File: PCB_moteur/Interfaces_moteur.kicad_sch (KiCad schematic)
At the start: 20 parts, among them J3 Conn_01x02, J4 SYS_SW_Conn_01x05_Header, J5 Conn_01x04_Socket, J7 Conn_02x06_Top_Bottom, U2 ISOW1044, U4 LSF0204PWR, U9 INA333xxDGK

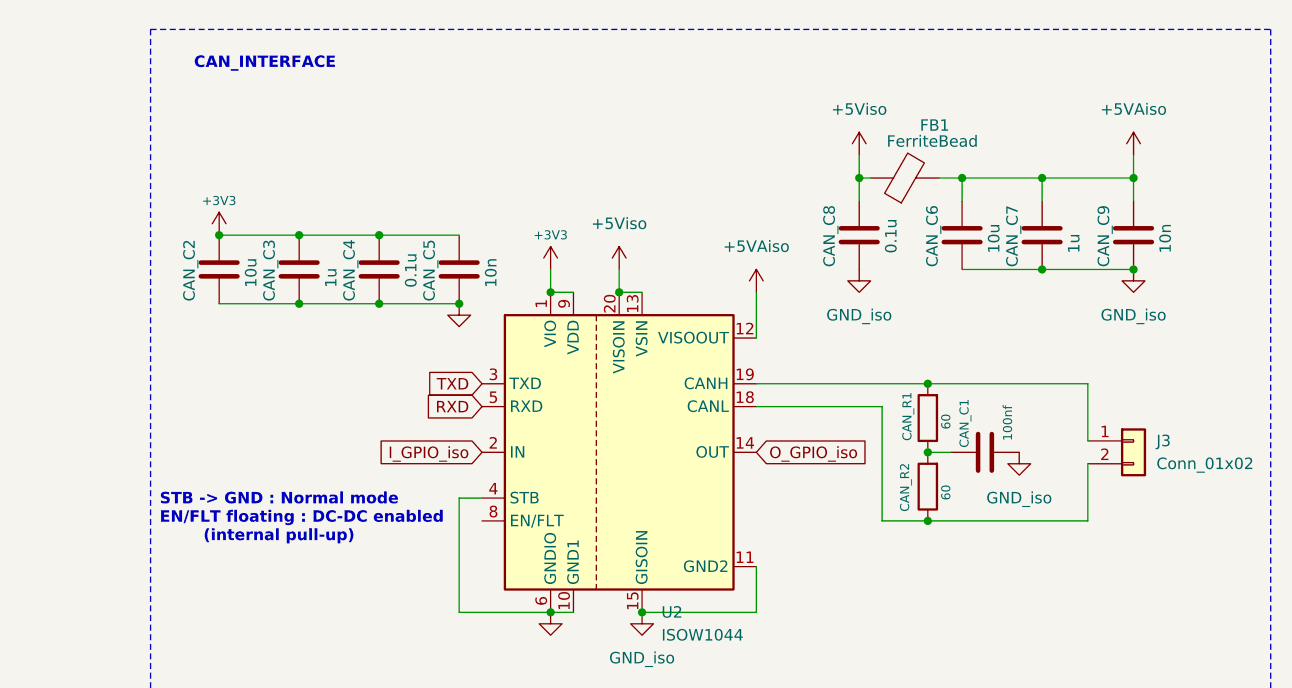
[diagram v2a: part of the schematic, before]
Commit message: wip: change 4 pyros -> 2 pyros
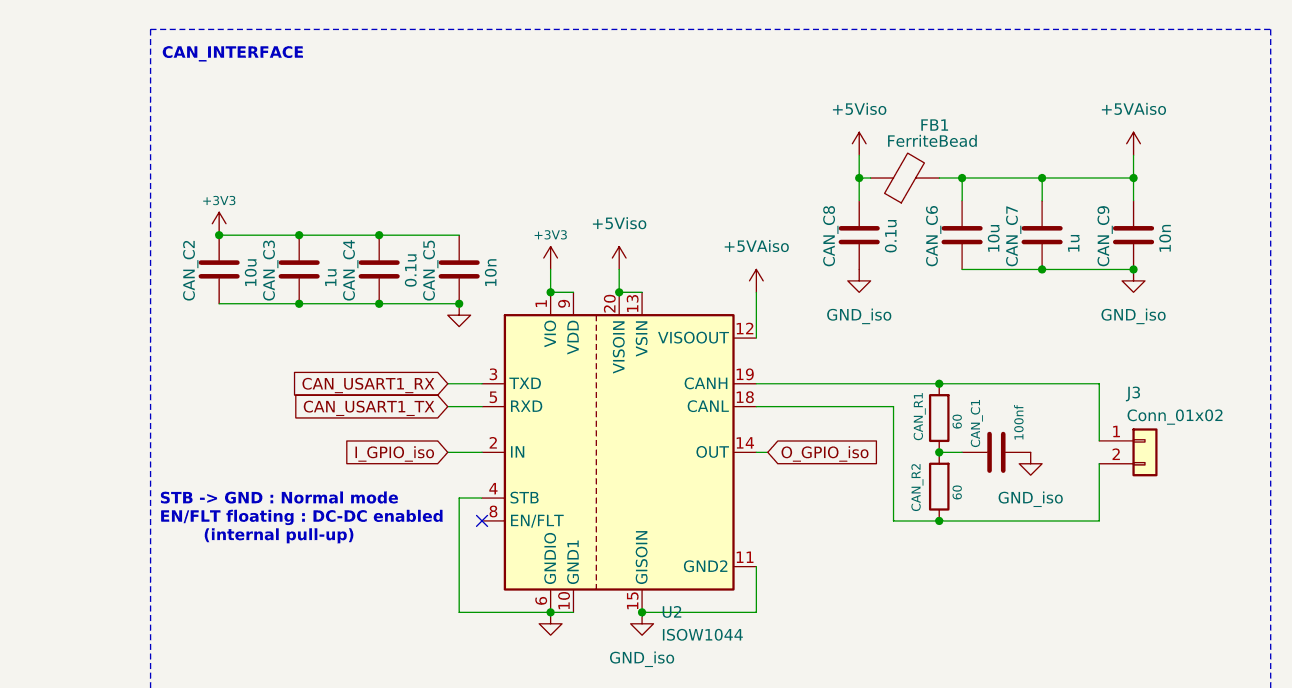
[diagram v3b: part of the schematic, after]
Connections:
- net RXD renamed CAN_USART1_TX
- net TXD renamed CAN_USART1_RX
- no-connect marks 0 -> 1
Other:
- moved on the sheet: CAN_C1, CAN_R1, CAN_R2, J3
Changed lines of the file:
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@@
 	(text "CAN_INTERFACE"
 		(exclude_from_sim no)
-		(at 162.306 40.132 0)
+		(at 158.75 39.116 0)
 		(effects
 			(font
@@
 	)
 	(junction
-		(at 243.84 82.55)
+		(at 245.11 82.55)
 		(diameter 0)
 		(color 0 0 0 0)
@@
 	)
 	(junction
-		(at 243.84 74.93)
+		(at 245.11 74.93)
 		(diameter 0)
 		(color 0 0 0 0)
@@
 	)
 	(junction
-		(at 243.84 90.17)
+		(at 245.11 90.17)
 		(diameter 0)
 		(color 0 0 0 0)
@@
 		(color 0 0 0 0)
 	)
+	(no_connect
+		(at 194.31 90.17)
+	)
 	(wire
 		(pts
@@
 	(wire
 		(pts
-			(xy 243.84 82.55) (xy 246.38 82.55)
+			(xy 245.11 82.55) (xy 247.65 82.55)
 		)
 		(stroke
@@
 	(wire
 		(pts
-			(xy 224.79 77.47) (xy 238.76 77.47)
+			(xy 224.79 77.47) (xy 240.03 77.47)
 		)
 		(stroke
@@
 	(wire
 		(pts
+			(xy 190.5 77.47) (xy 194.31 77.47)
+		)
+		(stroke
+			(width 0)
+			(type default)
+		)
+	)
+	(wire
+		(pts
 			(xy 60.96 102.87) (xy 64.77 102.87)
 		)
@@
 	(wire
 		(pts
-			(xy 238.76 77.47) (xy 238.76 90.17)
+			(xy 240.03 77.47) (xy 240.03 90.17)
 		)
 		(stroke
@@
 	(wire
 		(pts
-			(xy 243.84 74.93) (xy 261.62 74.93)
+			(xy 245.11 74.93) (xy 262.89 74.93)
 		)
 		(stroke
@@
 	(wire
 		(pts
+			(xy 226.06 82.55) (xy 224.79 82.55)
+		)
+		(stroke
+			(width 0)
+			(type default)
+		)
+	)
+	(wire
+		(pts
 			(xy 55.88 152.4) (xy 59.69 152.4)
 		)
@@
 	(wire
 		(pts
+			(xy 190.5 82.55) (xy 194.31 82.55)
+		)
+		(stroke
+			(width 0)
+			(type default)
+		)
+	)
+	(wire
+		(pts
 			(xy 81.28 102.87) (xy 77.47 102.87)
 		)
@@
 	(wire
 		(pts
-			(xy 224.79 74.93) (xy 243.84 74.93)
+			(xy 224.79 74.93) (xy 245.11 74.93)
 		)
 		(stroke
@@
 	(wire
 		(pts
-			(xy 261.62 90.17) (xy 261.62 83.82)
+			(xy 262.89 90.17) (xy 262.89 83.82)
 		)
 		(stroke
@@
 	(wire
 		(pts
+			(xy 190.5 74.93) (xy 194.31 74.93)
+		)
+		(stroke
+			(width 0)
+			(type default)
+		)
+	)
+	(wire
+		(pts
 			(xy 231.14 152.4) (xy 231.14 147.32)
 		)
@@
 	(wire
 		(pts
-			(xy 238.76 90.17) (xy 243.84 90.17)
+			(xy 240.03 90.17) (xy 245.11 90.17)
 		)
 		(stroke
@@
 	(wire
 		(pts
-			(xy 261.62 81.28) (xy 261.62 74.93)
+			(xy 262.89 81.28) (xy 262.89 74.93)
 		)
 		(stroke
@@
 	(wire
 		(pts
-			(xy 243.84 90.17) (xy 261.62 90.17)
+			(xy 245.11 90.17) (xy 262.89 90.17)
 		)
 		(stroke
@@
 		)
 	)
-	(global_label "TXD"
+	(global_label "CAN_USART1_RX"
 		(shape input)
-		(at 194.31 74.93 180)
+		(at 190.5 74.93 180)
 		(fields_autoplaced yes)
 		(effects
@@
 		)
 		(property "Intersheetrefs" "${INTERSHEET_REFS}"
-			(at 187.8777 74.93 0)
+			(at 172.3353 74.93 0)
 			(effects
 				(font
@@
 	(global_label "I_GPIO_iso"
 		(shape input)
-		(at 194.31 82.55 180)
+		(at 190.5 82.55 180)
 		(fields_autoplaced yes)
 		(effects
@@
 		)
 		(property "Intersheetrefs" "${INTERSHEET_REFS}"
-			(at 181.5276 82.55 0)
+			(at 177.7176 82.55 0)
 			(effects
 				(font
@@
 	(global_label "O_GPIO_iso"
 		(shape input)
-		(at 224.79 82.55 0)
+		(at 226.06 82.55 0)
 		(fields_autoplaced yes)
 		(effects
@@
 		)
 		(property "Intersheetrefs" "${INTERSHEET_REFS}"
-			(at 238.2981 82.55 0)
+			(at 239.5681 82.55 0)
 			(effects
 				(font
@@
 		)
 	)
-	(global_label "RXD"
+	(global_label "CAN_USART1_TX"
 		(shape input)
-		(at 194.31 77.47 180)
+		(at 190.5 77.47 180)
 		(fields_autoplaced yes)
 		(effects
@@
 		)
 		(property "Intersheetrefs" "${INTERSHEET_REFS}"
-			(at 187.5753 77.47 0)
+			(at 172.6377 77.47 0)
 			(effects
 				(font
@@
 	(symbol
 		(lib_id "Device:R")
-		(at 243.84 86.36 180)
+		(at 245.11 86.36 180)
 		(unit 1)
 		(exclude_from_sim no)
@@
 		(dnp no)
 		(property "Reference" "CAN_R2"
-			(at 241.3 89.154 90)
+			(at 242.57 89.154 90)
 			(effects
 				(font
@@
 		)
 		(property "Value" "60"
-			(at 245.872 87.884 90)
+			(at 247.142 87.884 90)
 			(effects
 				(font
@@
 		)
 		(property "Footprint" "Resistor_SMD:R_0805_2012Metric"
-			(at 245.618 86.36 90)
+			(at 246.888 86.36 90)
 			(effects
 				(font
@@
 		)
 		(property "Datasheet" "~"
-			(at 243.84 86.36 0)
+			(at 245.11 86.36 0)
 			(effects
 				(font
@@
 		)
 		(property "Description" ""
-			(at 243.84 86.36 0)
+			(at 245.11 86.36 0)
 			(effects
 				(font
@@
 	(symbol
 		(lib_id "power:GND1")
-		(at 254 82.55 0)
+		(at 255.27 82.55 0)
 		(unit 1)
 		(exclude_from_sim no)
@@
 		(fields_autoplaced yes)
 		(property "Reference" "#PWR014"
-			(at 254 88.9 0)
+			(at 255.27 88.9 0)
 			(effects
 				(font
@@
 		)
 		(property "Value" "GND_iso"
-			(at 254 87.63 0)
+			(at 255.27 87.63 0)
 			(effects
 				(font
@@
 		)
 		(property "Footprint" ""
-			(at 254 82.55 0)
+			(at 255.27 82.55 0)
 			(effects
 				(font
@@
 		)
 		(property "Datasheet" ""
-			(at 254 82.55 0)
+			(at 255.27 82.55 0)
 			(effects
 				(font
@@
 		)
 		(property "Description" "Power symbol creates a global label with name \"GND1\" , ground"
-			(at 254 82.55 0)
+			(at 255.27 82.55 0)
 			(effects
 				(font
@@
 	(symbol
 		(lib_id "Device:R")
-		(at 243.84 78.74 180)
+		(at 245.11 78.74 180)
 		(unit 1)
 		(exclude_from_sim no)
@@
 		(dnp no)
 		(property "Reference" "CAN_R1"
-			(at 241.554 81.28 90)
+			(at 242.824 81.28 90)
 			(effects
 				(font
@@
 		)
 		(property "Value" "60"
-			(at 245.872 80.01 90)
+			(at 247.142 80.01 90)
 			(effects
 				(font
@@
 		)
 		(property "Footprint" "Resistor_SMD:R_0805_2012Metric"
-			(at 245.618 78.74 90)
+			(at 246.888 78.74 90)
 			(effects
 				(font
@@
 		)
 		(property "Datasheet" "~"
-			(at 243.84 78.74 0)
+			(at 245.11 78.74 0)
 			(effects
 				(font
@@
 		)
 		(property "Description" ""
-			(at 243.84 78.74 0)
+			(at 245.11 78.74 0)
 			(effects
 				(font
@@
 	(symbol
 		(lib_id "Connector_Generic:Conn_01x02")
-		(at 266.7 81.28 0)
+		(at 267.97 81.28 0)
 		(unit 1)
 		(exclude_from_sim no)
@@
 		(on_board yes)
 		(dnp no)
-		(fields_autoplaced yes)
 		(property "Reference" "J3"
-			(at 269.24 81.2799 0)
+			(at 265.938 75.946 0)
 			(effects
 				(font
@@
 		)
 		(property "Value" "Conn_01x02"
-			(at 269.24 83.8199 0)
+			(at 265.938 78.486 0)
 			(effects
 				(font
@@
 		)
 		(property "Footprint" ""
-			(at 266.7 81.28 0)
+			(at 267.97 81.28 0)
 			(effects
 				(font
@@
 		)
 		(property "Datasheet" "~"
-			(at 266.7 81.28 0)
+			(at 267.97 81.28 0)
 			(effects
 				(font
@@
 		)
 		(property "Description" "Generic connector, single row, 01x02, script generated (kicad-library-utils/schlib/autogen/connector/)"
-			(at 266.7 81.28 0)
+			(at 267.97 81.28 0)
 			(effects
 				(font
@@
 	(symbol
 		(lib_id "Device:C")
-		(at 250.19 82.55 90)
+		(at 251.46 82.55 90)
 		(unit 1)
 		(exclude_from_sim no)
@@
 		(dnp no)
 		(property "Reference" "CAN_C1"
-			(at 247.904 82.042 0)
+			(at 249.174 82.042 0)
 			(effects
 				(font
@@
 		)
 		(property "Value" "100nf"
-			(at 252.73 81.28 0)
+			(at 254 81.28 0)
 			(effects
 				(font
@@
 		)
 		(property "Footprint" "Capacitor_SMD:C_0805_2012Metric"
-			(at 254 81.5848 0)
+			(at 255.27 81.5848 0)
 			(effects
 				(font
@@
 		)
 		(property "Datasheet" "~"
-			(at 250.19 82.55 0)
+			(at 251.46 82.55 0)
 			(effects
 				(font
@@
 		)
 		(property "Description" ""
-			(at 250.19 82.55 0)
+			(at 251.46 82.55 0)
 			(effects
 				(font

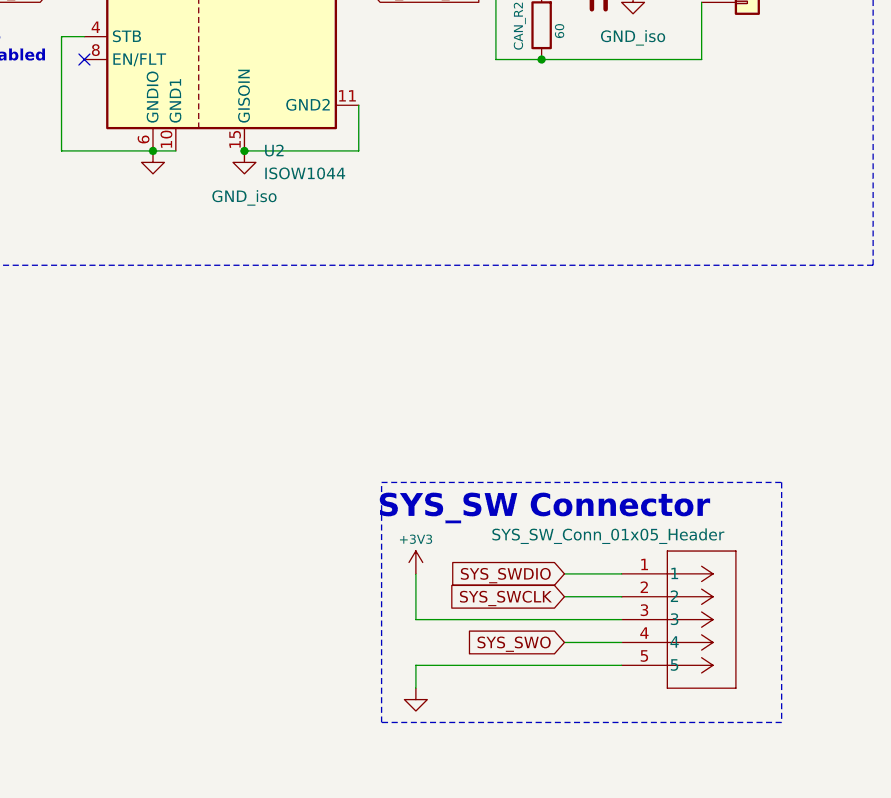
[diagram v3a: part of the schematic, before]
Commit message: fix: power supply + add LED RG + add mounting holes + change 6pins header SWD connector + pyros
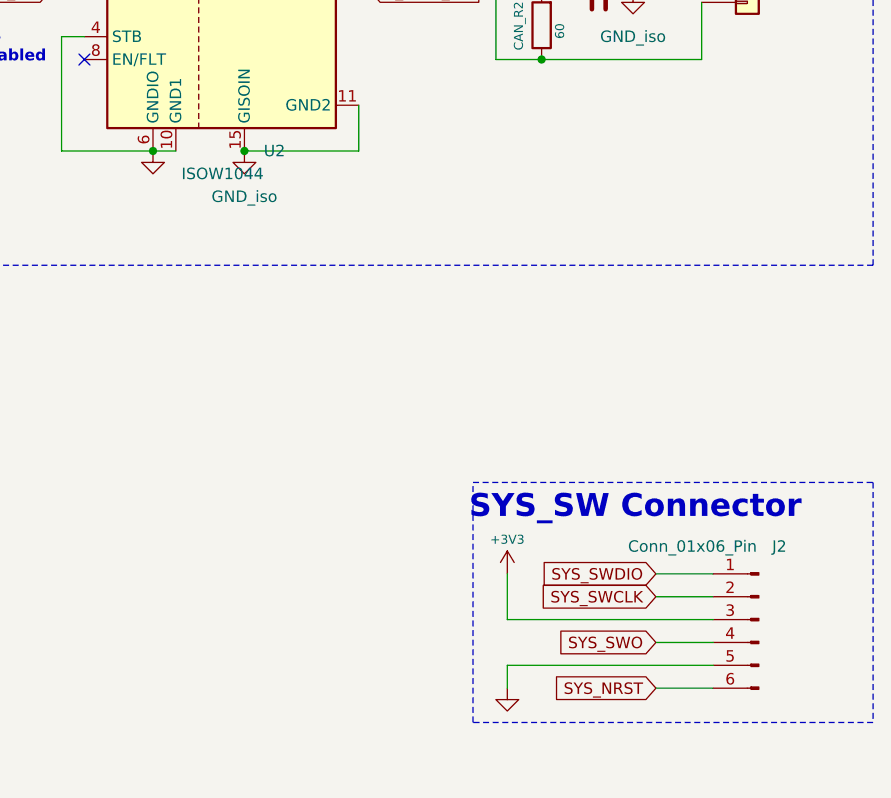
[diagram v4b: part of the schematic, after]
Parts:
- removed J4: SYS_SW_Conn_01x05_Header, Connector_PinHeader_2.54mm:PinHeader_1x05_P2.54mm_Vertical, symbol ODB2:705430004
- added J2: Conn_01x06_Pin, symbol Connector:Conn_01x06_Pin
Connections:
- net +3V3: now also J2.3 (Pin_3)
- net GND: now also J2.5 (Pin_5)
- net SYS_SWCLK: now also J2.2 (Pin_2)
- net SYS_SWDIO: now also J2.1 (Pin_1)
- net SYS_SWO: now also J2.4 (Pin_4)
- new net SYS_NRST: J2.6 (Pin_6)
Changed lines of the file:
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@@
 	(paper "A4")
 	(rectangle
-		(start 227.33 137.16)
-		(end 271.78 163.83)
+		(start 237.49 137.16)
+		(end 281.94 163.83)
 		(stroke
 			(width 0)
@@
 	(text "SYS_SW Connector"
 		(exclude_from_sim no)
-		(at 245.364 139.954 0)
+		(at 255.524 139.954 0)
 		(effects
 			(font
@@
 	(wire
 		(pts
-			(xy 254 152.4) (xy 231.14 152.4)
+			(xy 264.16 152.4) (xy 241.3 152.4)
 		)
 		(stroke
@@
 	(wire
 		(pts
-			(xy 247.65 149.86) (xy 254 149.86)
+			(xy 257.81 149.86) (xy 264.16 149.86)
 		)
 		(stroke
@@
 	(wire
 		(pts
-			(xy 231.14 157.48) (xy 231.14 160.02)
+			(xy 241.3 157.48) (xy 241.3 160.02)
 		)
 		(stroke
@@
 	(wire
 		(pts
+			(xy 257.81 160.02) (xy 264.16 160.02)
+		)
+		(stroke
+			(width 0)
+			(type default)
+		)
+	)
+	(wire
+		(pts
 			(xy 58.42 151.13) (xy 59.69 151.13)
 		)
@@
 	(wire
 		(pts
-			(xy 247.65 154.94) (xy 254 154.94)
+			(xy 257.81 154.94) (xy 264.16 154.94)
 		)
 		(stroke
@@
 	(wire
 		(pts
-			(xy 247.65 147.32) (xy 254 147.32)
+			(xy 257.81 147.32) (xy 264.16 147.32)
 		)
 		(stroke
@@
 	(wire
 		(pts
-			(xy 254 157.48) (xy 231.14 157.48)
+			(xy 264.16 157.48) (xy 241.3 157.48)
 		)
 		(stroke
@@
 	(wire
 		(pts
-			(xy 231.14 152.4) (xy 231.14 147.32)
+			(xy 241.3 152.4) (xy 241.3 147.32)
 		)
 		(stroke
@@
 	(global_label "SYS_SWO"
 		(shape input)
-		(at 247.65 154.94 180)
+		(at 257.81 154.94 180)
 		(fields_autoplaced yes)
 		(effects
@@
 		)
 		(property "Intersheetrefs" "${INTERSHEET_REFS}"
-			(at 236.1982 154.94 0)
+			(at 246.3582 154.94 0)
 			(effects
 				(font
@@
 		)
 	)
+	(global_label "SYS_NRST"
+		(shape input)
+		(at 257.81 160.02 180)
+		(fields_autoplaced yes)
+		(effects
+			(font
+				(size 1.27 1.27)
+				(thickness 0.1588)
+			)
+			(justify right)
+		)
+		(property "Intersheetrefs" "${INTERSHEET_REFS}"
+			(at 245.572 160.02 0)
+			(effects
+				(font
+					(size 1.27 1.27)
+				)
+				(justify right)
+				(hide yes)
+			)
+		)
+	)
 	(global_label "PWM_SERVO4"
 		(shape input)
@@
 	(global_label "SYS_SWDIO"
 		(shape input)
-		(at 247.65 147.32 180)
+		(at 257.81 147.32 180)
 		(fields_autoplaced yes)
 		(effects
@@
 		)
 		(property "Intersheetrefs" "${INTERSHEET_REFS}"
-			(at 234.3234 147.32 0)
+			(at 244.4834 147.32 0)
 			(effects
 				(font
@@
 	(global_label "SYS_SWCLK"
 		(shape input)
-		(at 247.65 149.86 180)
+		(at 257.81 149.86 180)
 		(fields_autoplaced yes)
 		(effects
@@
 		)
 		(property "Intersheetrefs" "${INTERSHEET_REFS}"
-			(at 233.9606 149.86 0)
+			(at 244.1206 149.86 0)
 			(effects
 				(font
@@
 	)
 	(symbol
+		(lib_id "Connector:Conn_01x06_Pin")
+		(at 269.24 152.4 0)
+		(mirror y)
+		(unit 1)
+		(exclude_from_sim no)
+		(in_bom yes)
+		(on_board yes)
+		(dnp no)
+		(property "Reference" "J2"
+			(at 271.526 144.272 0)
+			(effects
+				(font
+					(size 1.27 1.27)
+				)
+			)
+		)
+		(property "Value" "Conn_01x06_Pin"
+			(at 261.874 144.272 0)
+			(effects
+				(font
+					(size 1.27 1.27)
+				)
+			)
+		)
+		(property "Footprint" ""
+			(at 269.24 152.4 0)
+			(effects
+				(font
+					(size 1.27 1.27)
+				)
+				(hide yes)
+			)
+		)
+		(property "Datasheet" "~"
+			(at 269.24 152.4 0)
+			(effects
+				(font
+					(size 1.27 1.27)
+				)
+				(hide yes)
+			)
+		)
+		(property "Description" "Generic connector, single row, 01x06, script generated"
+			(at 269.24 152.4 0)
+			(effects
+				(font
+					(size 1.27 1.27)
+				)
+				(hide yes)
+			)
+		)
+		(pin "1"
+		)
+		(pin "4"
+		)
+		(pin "6"
+		)
+		(pin "5"
+		)
+		(pin "2"
+		)
+		(pin "3"
+		)
+		(instances
+			(project ""
+				(path "/b0d87684-7b1c-41d8-8358-755aa327573e/a8ed0c04-b51e-4eec-84d1-0b2303d57d27"
+					(reference "J2")
+					(unit 1)
+				)
+			)
+		)
+	)
+	(symbol
 		(lib_name "+5V_1")
 		(lib_id "power:+5V")
@@
 	(symbol
 		(lib_id "power:+3V3")
-		(at 231.14 147.32 0)
+		(at 241.3 147.32 0)
 		(unit 1)
 		(exclude_from_sim no)
@@
 		(dnp no)
 		(property "Reference" "#PWR046"
-			(at 231.14 151.13 0)
+			(at 241.3 151.13 0)
 			(effects
 				(font
@@
 		)
 		(property "Value" "+3V3"
-			(at 231.14 143.51 0)
+			(at 241.3 143.51 0)
 			(effects
 				(font
@@
 		)
 		(property "Footprint" ""
-			(at 231.14 147.32 0)
+			(at 241.3 147.32 0)
 			(effects
 				(font
@@
 		)
 		(property "Datasheet" ""
-			(at 231.14 147.32 0)
+			(at 241.3 147.32 0)
 			(effects
 				(font
@@
 		)
 		(property "Description" ""
-			(at 231.14 147.32 0)
+			(at 241.3 147.32 0)
 			(effects
 				(font
@@
 	)
 	(symbol
-		(lib_id "ODB2:705430004")
-		(at 254 147.32 0)
-		(unit 1)
-		(exclude_from_sim no)
-		(in_bom yes)
-		(on_board yes)
-		(dnp no)
-		(property "Reference" "J4"
-			(at 256.794 140.208 0)
-			(effects
-				(font
-					(size 1.524 1.524)
-				)
-				(justify left)
-				(hide yes)
-			)
-		)
-		(property "Value" "SYS_SW_Conn_01x05_Header"
-			(at 239.522 143.002 0)
-			(effects
-				(font
-					(size 1.27 1.27)
-				)
-				(justify left)
-			)
-		)
-		(property "Footprint" "Connector_PinHeader_2.54mm:PinHeader_1x05_P2.54mm_Vertical"
-			(at 244.094 140.716 0)
-			(effects
-				(font
-					(size 1.27 1.27)
-					(italic yes)
-				)
-				(hide yes)
-			)
-		)
-		(property "Datasheet" "705430004"
-			(at 272.796 143.764 0)
-			(effects
-				(font
-					(size 1.27 1.27)
-					(italic yes)
-				)
-				(hide yes)
-			)
-		)
-		(property "Description" ""
-			(at 254 147.32 0)
-			(effects
-				(font
-					(size 1.27 1.27)
-				)
-				(hide yes)
-			)
-		)
-		(pin "2"
-		)
-		(pin "4"
-		)
-		(pin "1"
-		)
-		(pin "5"
-		)
-		(pin "3"
-		)
-		(instances
-			(project "PCB_moteur"
-				(path "/b0d87684-7b1c-41d8-8358-755aa327573e/a8ed0c04-b51e-4eec-84d1-0b2303d57d27"
-					(reference "J4")
-					(unit 1)
-				)
-			)
-		)
-	)
-	(symbol
 		(lib_id "power:GND")
 		(at 44.45 142.24 270)
@@
 		(on_board yes)
 		(dnp no)
-		(fields_autoplaced yes)
 		(property "Reference" "U2"
 			(at 214.2333 100.33 0)
@@
 					(size 1.27 1.27)
 				)
-				(justify left)
+				(justify right)
 			)
 		)
@@
 	(symbol
 		(lib_id "power:GND")
-		(at 231.14 160.02 0)
+		(at 241.3 160.02 0)
 		(unit 1)
 		(exclude_from_sim no)
@@
 		(fields_autoplaced yes)
 		(property "Reference" "#PWR027"
-			(at 231.14 166.37 0)
+			(at 241.3 166.37 0)
 			(effects
 				(font
@@
 		)
 		(property "Value" "GND"
-			(at 231.14 165.1 0)
+			(at 241.3 165.1 0)
 			(effects
 				(font
@@
 		)
 		(property "Footprint" ""
-			(at 231.14 160.02 0)
+			(at 241.3 160.02 0)
 			(effects
 				(font
@@
 		)
 		(property "Datasheet" ""
-			(at 231.14 160.02 0)
+			(at 241.3 160.02 0)
 			(effects
 				(font
@@
 		)
 		(property "Description" ""
-			(at 231.14 160.02 0)
+			(at 241.3 160.02 0)
 			(effects
 				(font
